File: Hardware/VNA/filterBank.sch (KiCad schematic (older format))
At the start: 18 parts, among them U10 74AHC1G04, U11 PE42440, U12 SN74LVC1G139, U13 PE42440

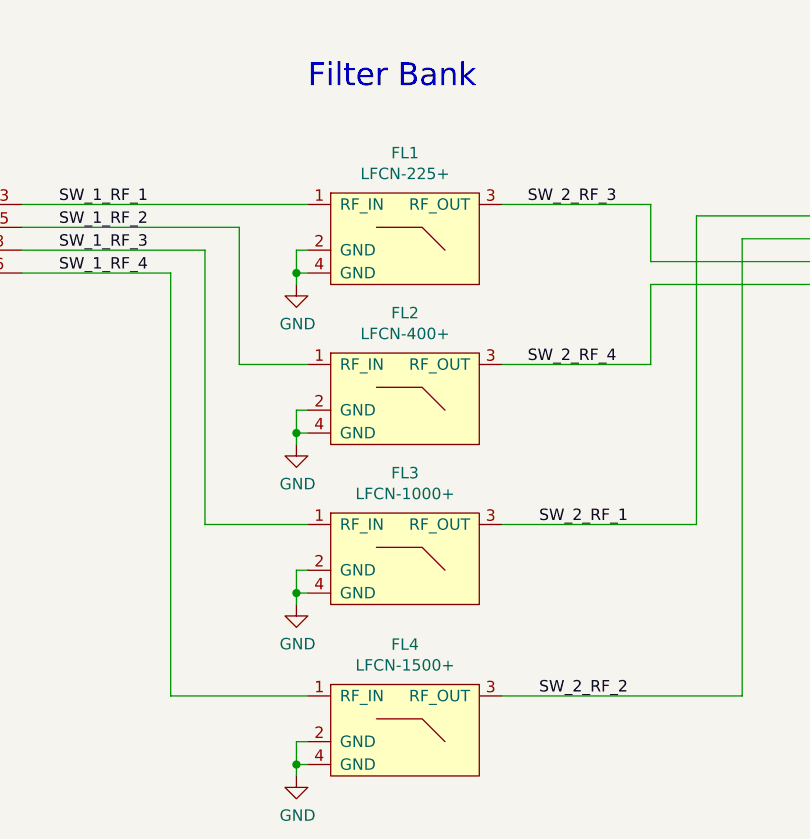
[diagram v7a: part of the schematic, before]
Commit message: FW for V0 init, functinal diagram / schematic updated freq ranges
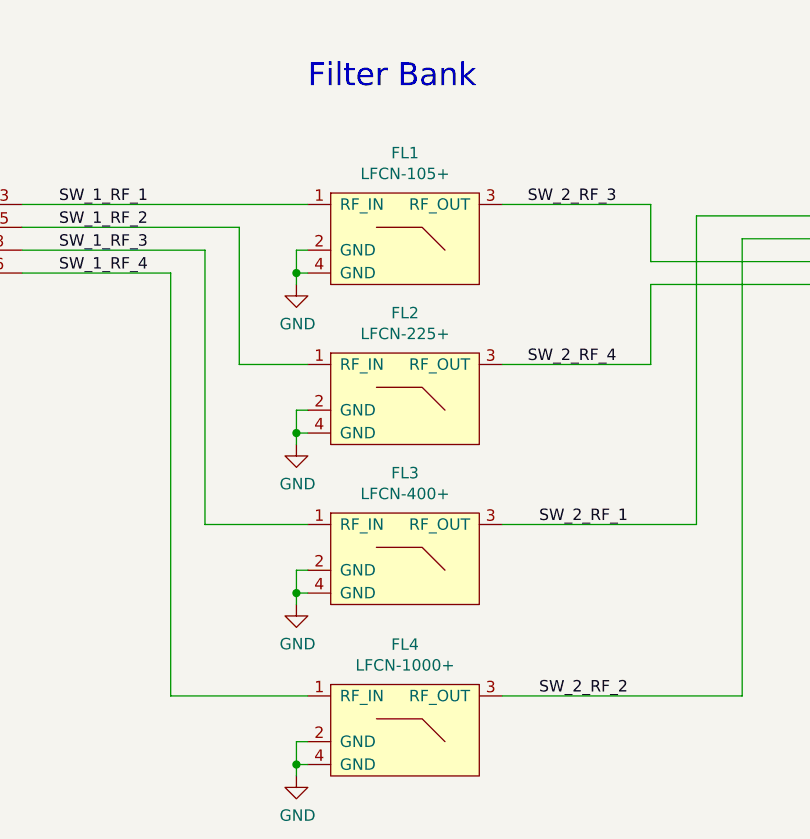
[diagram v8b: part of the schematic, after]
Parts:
- FL1: value LFCN-225+ -> LFCN-105+
- FL2: value LFCN-400+ -> LFCN-225+
- FL3: value LFCN-1000+ -> LFCN-400+
- FL4: value LFCN-1500+ -> LFCN-1000+
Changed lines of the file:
@@
 P 5700 2350
 F 0 "FL1" H 5725 2675 50  0000 C CNN
-F 1 "LFCN-225+" H 5725 2584 50  0000 C CNN
+F 1 "LFCN-105+" H 5725 2584 50  0000 C CNN
 F 2 "VNA_Footprints:FV1206" H 5700 2500 50  0001 C CNN
 F 3 "" H 5700 2500 50  0001 C CNN
@@
 P 5700 3050
 F 0 "FL2" H 5725 3375 50  0000 C CNN
-F 1 "LFCN-400+" H 5725 3284 50  0000 C CNN
+F 1 "LFCN-225+" H 5725 3284 50  0000 C CNN
 F 2 "VNA_Footprints:FV1206" H 5700 3200 50  0001 C CNN
 F 3 "" H 5700 3200 50  0001 C CNN
@@
 P 5700 3750
 F 0 "FL3" H 5725 4075 50  0000 C CNN
-F 1 "LFCN-1000+" H 5725 3984 50  0000 C CNN
+F 1 "LFCN-400+" H 5725 3984 50  0000 C CNN
 F 2 "VNA_Footprints:FV1206" H 5700 3900 50  0001 C CNN
 F 3 "" H 5700 3900 50  0001 C CNN
@@
 P 5700 4500
 F 0 "FL4" H 5725 4825 50  0000 C CNN
-F 1 "LFCN-1500+" H 5725 4734 50  0000 C CNN
+F 1 "LFCN-1000+" H 5725 4734 50  0000 C CNN
 F 2 "VNA_Footprints:FV1206" H 5700 4650 50  0001 C CNN
 F 3 "" H 5700 4650 50  0001 C CNN
